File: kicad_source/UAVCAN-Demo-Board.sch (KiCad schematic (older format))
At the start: 35 parts, among them CN1 ARDUINO_NANO_33, CN2 691322310004, CN3 GH_SM04B-GHS-TB, CN4 GH_SM04B-GHS-TB, CN5 691322310004, CN6 691322310004, SW1 TAST_VER, U1 MCP2515, U2 SN65VHD232, U3 DS18B20, Y1 16 MHz

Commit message: started layout, added THT parts
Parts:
- CN5, CN6: footprint CON_wuerth:WR-TBL_691322310004 -> pin_headers:Pin_Header_Straight_1x04
- D1, D2, D3, D5, D6, D7: footprint LEDs:LED_0603 -> LEDs:LED-5MM
- RV1: footprint (none) -> potentiometers:Potentiometer_Trimmer-Piher_PT15-V12-5_horizontal
- U1: footprint SOIC:SOIC-18_7.5x11.6mm_Pitch1.27mm -> DIP:DIP-18_W7.62mm
- U2: footprint SOIC:SOIC-8_3.9x4.9mm_Pitch1.27mm -> DIP:DIP-8_W7.62mm
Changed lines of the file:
@@
 F 0 "U2" H 4775 2887 60  0000 C CNN
 F 1 "SN65VHD232" H 4775 2781 60  0000 C CNN
-F 2 "SOIC:SOIC-8_3.9x4.9mm_Pitch1.27mm" H 5100 1950 60  0001 C CNN
+F 2 "DIP:DIP-8_W7.62mm" H 5100 1950 60  0001 C CNN
 F 3 "" H 4250 2150 60  0000 C CNN
 	1    4250 2000
@@
 F 0 "D1" H 6200 3095 50  0000 C CNN
 F 1 "150060GS75000" H 6200 3186 50  0000 C CNN
-F 2 "LEDs:LED_0603" V 6200 3300 50  0001 C CNN
+F 2 "LEDs:LED-5MM" V 6200 3300 50  0001 C CNN
 F 3 "" V 6200 3300 50  0000 C CNN
 	1    6200 3300
@@
 F 0 "D2" H 6200 3445 50  0000 C CNN
 F 1 "150060RS75000" H 6200 3536 50  0000 C CNN
-F 2 "LEDs:LED_0603" V 6200 3650 50  0001 C CNN
+F 2 "LEDs:LED-5MM" V 6200 3650 50  0001 C CNN
 F 3 "" V 6200 3650 50  0000 C CNN
 	1    6200 3650
@@
 F 0 "D3" H 6200 3795 50  0000 C CNN
 F 1 "150060YS75000" H 6200 3886 50  0000 C CNN
-F 2 "LEDs:LED_0603" V 6200 4000 50  0001 C CNN
+F 2 "LEDs:LED-5MM" V 6200 4000 50  0001 C CNN
 F 3 "" V 6200 4000 50  0000 C CNN
 	1    6200 4000
@@
 F 0 "U1" H 2900 4825 50  0000 C CNN
 F 1 "MCP2515" H 2900 4734 50  0000 C CNN
-F 2 "SOIC:SOIC-18_7.5x11.6mm_Pitch1.27mm" H 2900 4100 50  0001 C CNN
+F 2 "DIP:DIP-18_W7.62mm" H 2900 4100 50  0001 C CNN
 F 3 "" H 2900 4100 50  0001 C CNN
 	1    2900 4100
@@
 F 0 "D5" H 6200 4195 50  0000 C CNN
 F 1 "150060YS75000" H 6200 4286 50  0000 C CNN
-F 2 "LEDs:LED_0603" V 6200 4400 50  0001 C CNN
+F 2 "LEDs:LED-5MM" V 6200 4400 50  0001 C CNN
 F 3 "" V 6200 4400 50  0000 C CNN
 	1    6200 4400
@@
 F 0 "D6" H 6200 4595 50  0000 C CNN
 F 1 "150060YS75000" H 6200 4686 50  0000 C CNN
-F 2 "LEDs:LED_0603" V 6200 4800 50  0001 C CNN
+F 2 "LEDs:LED-5MM" V 6200 4800 50  0001 C CNN
 F 3 "" V 6200 4800 50  0000 C CNN
 	1    6200 4800
@@
 F 0 "D7" H 6200 4995 50  0000 C CNN
 F 1 "150060YS75000" H 6200 5086 50  0000 C CNN
-F 2 "LEDs:LED_0603" V 6200 5200 50  0001 C CNN
+F 2 "LEDs:LED-5MM" V 6200 5200 50  0001 C CNN
 F 3 "" V 6200 5200 50  0000 C CNN
 	1    6200 5200
@@
 F 0 "RV1" V 6104 6372 50  0000 R CNN
 F 1 "POT" V 6195 6372 50  0000 R CNN
-F 2 "" H 6150 6450 50  0000 C CNN
+F 2 "potentiometers:Potentiometer_Trimmer-Piher_PT15-V12-5_horizontal" H 6150 6450 50  0001 C CNN
 F 3 "" H 6150 6450 50  0000 C CNN
 	1    6150 6450
@@
 F 0 "CN5" H 2328 1541 50  0000 L CNN
 F 1 "691322310004" H 2328 1450 50  0000 L CNN
-F 2 "CON_wuerth:WR-TBL_691322310004" H 2250 1500 50  0001 C CNN
+F 2 "pin_headers:Pin_Header_Straight_1x04" H 2250 1500 50  0001 C CNN
 F 3 "" H 2250 1500 50  0000 C CNN
 	1    2250 1500
@@
 F 0 "CN6" H 2328 2491 50  0000 L CNN
 F 1 "691322310004" H 2328 2400 50  0000 L CNN
-F 2 "CON_wuerth:WR-TBL_691322310004" H 2250 2450 50  0001 C CNN
+F 2 "pin_headers:Pin_Header_Straight_1x04" H 2250 2450 50  0001 C CNN
 F 3 "" H 2250 2450 50  0000 C CNN
 	1    2250 2450

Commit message: switched to THT parts
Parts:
- C1: footprint capacitors:C_0603 -> Capacitor_THT:C_Disc_D3.8mm_W2.6mm_P2.50mm
- C2, C3, C4: footprint (none) -> Capacitor_THT:C_Disc_D3.8mm_W2.6mm_P2.50mm
- D4: footprint diodes:SOD-123 -> Diode_THT:D_DO-41_SOD81_P7.62mm_Horizontal
- R1, R2, R3, R4, R5, R6, R7, R8: footprint resistors:R_0603 -> Resistor_THT:R_Axial_DIN0207_L6.3mm_D2.5mm_P7.62mm_Horizontal
- RV1: footprint potentiometers:Potentiometer_Trimmer-Piher_PT15-V12-5_horizontal -> Potentiometer_THT:Potentiometer_Piher_PT-10-V10_Vertical
- Y1: footprint (none) -> crystals:Crystal_HC49-U_Vertical
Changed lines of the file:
@@
 F 0 "R4" H 6659 1996 50  0000 L CNN
 F 1 "DNI" H 6659 1905 50  0000 L CNN
-F 2 "resistors:R_0603" H 6600 1800 50  0001 C CNN
+F 2 "Resistor_THT:R_Axial_DIN0207_L6.3mm_D2.5mm_P7.62mm_Horizontal" H 6600 1800 50  0001 C CNN
 F 3 "" H 6600 1950 50  0000 C CNN
 	1    6600 1950
@@
 F 0 "C1" H 3892 1246 50  0000 L CNN
 F 1 "100nF" H 3892 1155 50  0000 L CNN
-F 2 "capacitors:C_0603" H 3800 1050 50  0001 C CNN
+F 2 "Capacitor_THT:C_Disc_D3.8mm_W2.6mm_P2.50mm" H 3800 1050 50  0001 C CNN
 F 3 "" H 3800 1200 50  0000 C CNN
 	1    3800 1200
@@
 F 0 "D4" H 10200 3605 50  0000 C CNN
 F 1 "DNI" H 10200 3514 50  0000 C CNN
-F 2 "diodes:SOD-123" V 10200 3400 50  0001 C CNN
+F 2 "Diode_THT:D_DO-41_SOD81_P7.62mm_Horizontal" V 10200 3400 50  0001 C CNN
 F 3 "" V 10200 3400 50  0000 C CNN
 	1    10200 3400
@@
 F 0 "R1" H 5709 3346 50  0000 L CNN
 F 1 "1k" H 5709 3255 50  0000 L CNN
-F 2 "resistors:R_0603" H 5650 3150 50  0001 C CNN
+F 2 "Resistor_THT:R_Axial_DIN0207_L6.3mm_D2.5mm_P7.62mm_Horizontal" H 5650 3150 50  0001 C CNN
 F 3 "" H 5650 3300 50  0000 C CNN
 	1    5650 3300
@@
 F 0 "R2" H 5709 3696 50  0000 L CNN
 F 1 "1k" H 5709 3605 50  0000 L CNN
-F 2 "resistors:R_0603" H 5650 3500 50  0001 C CNN
+F 2 "Resistor_THT:R_Axial_DIN0207_L6.3mm_D2.5mm_P7.62mm_Horizontal" H 5650 3500 50  0001 C CNN
 F 3 "" H 5650 3650 50  0000 C CNN
 	1    5650 3650
@@
 F 0 "R3" H 5709 4046 50  0000 L CNN
 F 1 "2k" H 5709 3955 50  0000 L CNN
-F 2 "resistors:R_0603" H 5650 3850 50  0001 C CNN
+F 2 "Resistor_THT:R_Axial_DIN0207_L6.3mm_D2.5mm_P7.62mm_Horizontal" H 5650 3850 50  0001 C CNN
 F 3 "" H 5650 4000 50  0000 C CNN
 	1    5650 4000
@@
 F 0 "Y1" H 3950 4925 50  0000 C CNN
 F 1 "16 MHz" H 3950 4834 50  0000 C CNN
-F 2 "" H 3950 4700 50  0000 C CNN
+F 2 "crystals:Crystal_HC49-U_Vertical" H 3950 4700 50  0001 C CNN
 F 3 "" H 3950 4700 50  0000 C CNN
 	1    3950 4700
@@
 F 0 "C2" H 3692 4896 50  0000 L CNN
 F 1 "18pF" H 3692 4805 50  0000 L CNN
-F 2 "" H 3550 4700 50  0001 C CNN
+F 2 "Capacitor_THT:C_Disc_D3.8mm_W2.6mm_P2.50mm" H 3550 4700 50  0001 C CNN
 F 3 "" H 3600 4850 50  0000 C CNN
 	1    3600 4850
@@
 F 0 "C4" H 4342 4896 50  0000 L CNN
 F 1 "18pF" H 4342 4805 50  0000 L CNN
-F 2 "" H 4200 4700 50  0001 C CNN
+F 2 "Capacitor_THT:C_Disc_D3.8mm_W2.6mm_P2.50mm" H 4200 4700 50  0001 C CNN
 F 3 "" H 4250 4850 50  0000 C CNN
 	1    4250 4850
@@
 F 0 "C3" H 4142 3796 50  0000 L CNN
 F 1 "100nF" H 4142 3705 50  0000 L CNN
-F 2 "" H 4000 3600 50  0001 C CNN
+F 2 "Capacitor_THT:C_Disc_D3.8mm_W2.6mm_P2.50mm" H 4000 3600 50  0001 C CNN
 F 3 "" H 4050 3750 50  0000 C CNN
 	1    4050 3750
@@
 F 0 "R5" H 5709 4446 50  0000 L CNN
 F 1 "1k" H 5709 4355 50  0000 L CNN
-F 2 "resistors:R_0603" H 5650 4250 50  0001 C CNN
+F 2 "Resistor_THT:R_Axial_DIN0207_L6.3mm_D2.5mm_P7.62mm_Horizontal" H 5650 4250 50  0001 C CNN
 F 3 "" H 5650 4400 50  0000 C CNN
 	1    5650 4400
@@
 F 0 "R6" H 5709 4846 50  0000 L CNN
 F 1 "1k" H 5709 4755 50  0000 L CNN
-F 2 "resistors:R_0603" H 5650 4650 50  0001 C CNN
+F 2 "Resistor_THT:R_Axial_DIN0207_L6.3mm_D2.5mm_P7.62mm_Horizontal" H 5650 4650 50  0001 C CNN
 F 3 "" H 5650 4800 50  0000 C CNN
 	1    5650 4800
@@
 F 0 "R7" H 5709 5246 50  0000 L CNN
 F 1 "1k" H 5709 5155 50  0000 L CNN
-F 2 "resistors:R_0603" H 5650 5050 50  0001 C CNN
+F 2 "Resistor_THT:R_Axial_DIN0207_L6.3mm_D2.5mm_P7.62mm_Horizontal" H 5650 5050 50  0001 C CNN
 F 3 "" H 5650 5200 50  0000 C CNN
 	1    5650 5200
@@
 F 0 "RV1" V 6104 6372 50  0000 R CNN
 F 1 "POT" V 6195 6372 50  0000 R CNN
-F 2 "potentiometers:Potentiometer_Trimmer-Piher_PT15-V12-5_horizontal" H 6150 6450 50  0001 C CNN
+F 2 "Potentiometer_THT:Potentiometer_Piher_PT-10-V10_Vertical" H 6150 6450 50  0001 C CNN
 F 3 "" H 6150 6450 50  0000 C CNN
 	1    6150 6450
@@
 F 0 "R8" H 8009 4246 50  0000 L CNN
 F 1 "10k" H 8009 4155 50  0000 L CNN
-F 2 "resistors:R_0603" H 7950 4050 50  0001 C CNN
+F 2 "Resistor_THT:R_Axial_DIN0207_L6.3mm_D2.5mm_P7.62mm_Horizontal" H 7950 4050 50  0001 C CNN
 F 3 "" H 7950 4200 50  0000 C CNN
 	1    7950 4200

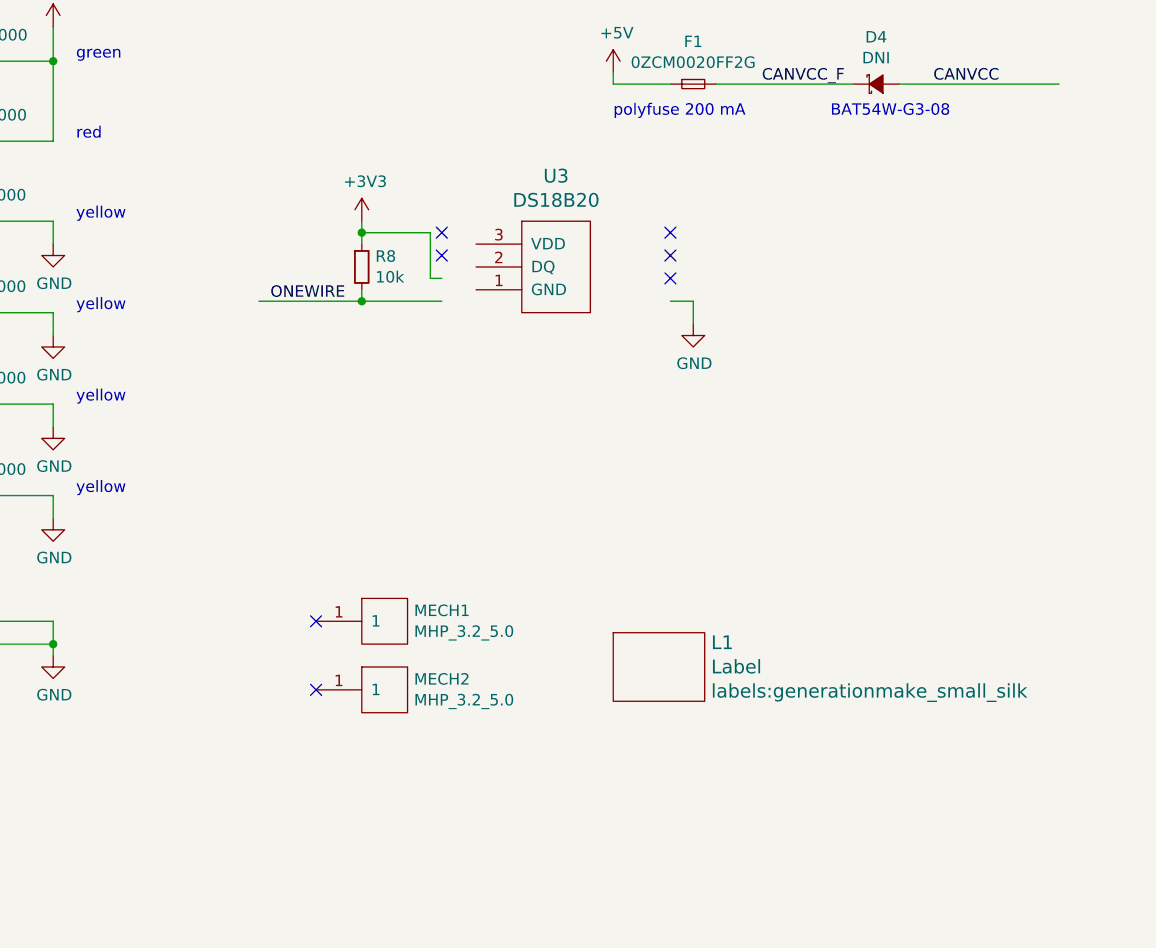
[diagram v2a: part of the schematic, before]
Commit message: changed DS18B20 to TO-92, cleaned up layout, added labels
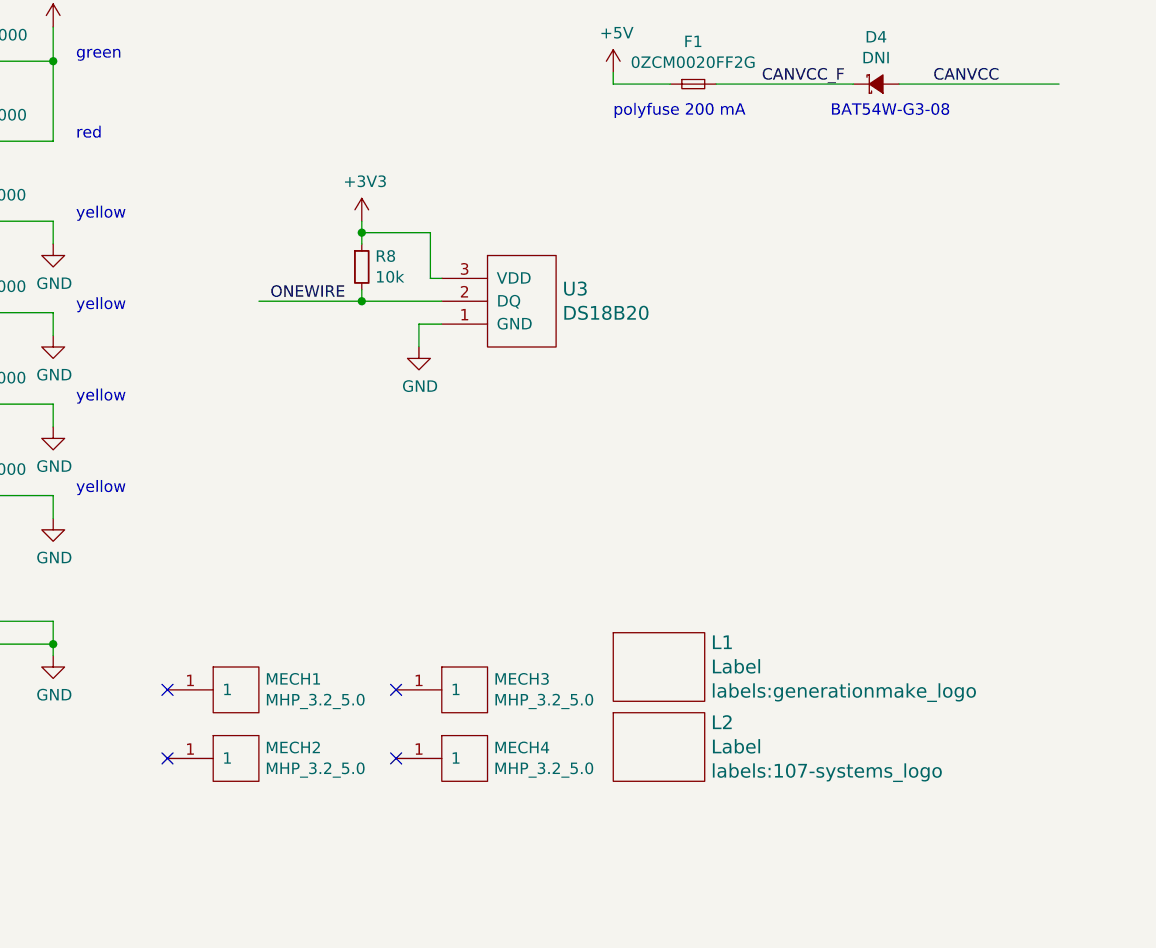
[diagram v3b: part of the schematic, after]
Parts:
- added L2: Label, labels:107-systems_logo, symbol devices:Label
- added MECH3, MECH4: MHP_3.2_5.0, MECH_mounting_holes:MHP_3.2_5.0, symbol MECH_mounting-holes:MHP_3.2_5.0
- F1: footprint resistors:R_0603 -> Resistor_THT:R_Axial_DIN0207_L6.3mm_D2.5mm_P5.08mm_Vertical
- L1: footprint labels:generationmake_small_silk -> labels:generationmake_logo
- U3: footprint SOIC:SOIC-8_3.9x4.9mm_Pitch1.27mm -> Package_TO_SOT_THT:TO-92
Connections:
- no-connect marks 16 -> 13
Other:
- moved on the sheet: MECH1, MECH2
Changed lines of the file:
@@
 F 0 "L1" H 9478 6056 60  0000 L CNN
 F 1 "Label" H 9478 5950 60  0000 L CNN
-F 2 "labels:generationmake_small_silk" H 9478 5844 60  0000 L CNN
+F 2 "labels:generationmake_logo" H 9478 5844 60  0000 L CNN
 F 3 "" H 9250 5950 60  0000 C CNN
 	1    9250 5950
@@
 F 0 "F1" H 9400 3585 50  0000 C CNN
 F 1 "0ZCM0020FF2G" H 9400 3494 50  0000 C CNN
-F 2 "resistors:R_0603" H 9400 3400 50  0001 C CNN
+F 2 "Resistor_THT:R_Axial_DIN0207_L6.3mm_D2.5mm_P5.08mm_Vertical" H 9400 3400 50  0001 C CNN
 F 3 "" H 9400 3400 50  0000 C CNN
 	1    9400 3400
@@
 L MECH_mounting-holes:MHP_3.2_5.0 MECH1
 U 1 1 5FF35FFC
-P 8050 5750
-F 0 "MECH1" H 8178 5796 50  0000 L CNN
-F 1 "MHP_3.2_5.0" H 8178 5705 50  0000 L CNN
-F 2 "MECH_mounting_holes:MHP_3.2_5.0" H 7950 5800 50  0001 C CNN
-F 3 "" H 8050 5750 50  0001 C CNN
-	1    8050 5750
-	1    0    0    -1
-$EndComp
-NoConn ~ 7750 5750
+P 7400 6050
+F 0 "MECH1" H 7528 6096 50  0000 L CNN
+F 1 "MHP_3.2_5.0" H 7528 6005 50  0000 L CNN
+F 2 "MECH_mounting_holes:MHP_3.2_5.0" H 7300 6100 50  0001 C CNN
+F 3 "" H 7400 6050 50  0001 C CNN
+	1    7400 6050
+	1    0    0    -1
+$EndComp
+NoConn ~ 7100 6050
 $Comp
 L MECH_mounting-holes:MHP_3.2_5.0 MECH2
 U 1 1 5FF376EB
-P 8050 6050
-F 0 "MECH2" H 8178 6096 50  0000 L CNN
-F 1 "MHP_3.2_5.0" H 8178 6005 50  0000 L CNN
-F 2 "MECH_mounting_holes:MHP_3.2_5.0" H 7950 6100 50  0001 C CNN
-F 3 "" H 8050 6050 50  0001 C CNN
-	1    8050 6050
-	1    0    0    -1
-$EndComp
-NoConn ~ 7750 6050
+P 7400 6350
+F 0 "MECH2" H 7528 6396 50  0000 L CNN
+F 1 "MHP_3.2_5.0" H 7528 6305 50  0000 L CNN
+F 2 "MECH_mounting_holes:MHP_3.2_5.0" H 7300 6400 50  0001 C CNN
+F 3 "" H 7400 6350 50  0001 C CNN
+	1    7400 6350
+	1    0    0    -1
+$EndComp
+NoConn ~ 7100 6350
 Text Notes 10000 3550 0    50   ~ 0
  BAT54W-G3-08
@@
 I2C_SCL
 $Comp
-L IC_sensor:DS18B20 U3
-U 1 1 60516299
-P 8800 4200
-F 0 "U3" H 8800 4597 60  0000 C CNN
-F 1 "DS18B20" H 8800 4491 60  0000 C CNN
-F 2 "SOIC:SOIC-8_3.9x4.9mm_Pitch1.27mm" H 8700 4350 60  0001 C CNN
-F 3 "" H 8800 4200 60  0000 C CNN
-	1    8800 4200
-	1    0    0    -1
-$EndComp
-$Comp
 L devices:R_0603 R?
 U 1 1 60516B88
@@
 L power-supply:GND #PWR?
 U 1 1 6053070B
-P 9400 4450
+P 8200 4550
 AR Path="/5FD58A5B/6053070B" Ref="#PWR?"  Part="1"
 AR Path="/6053070B" Ref="#PWR029"  Part="1"
-F 0 "#PWR029" H 9400 4200 50  0001 C CNN
-F 1 "GND" H 9405 4277 50  0000 C CNN
-F 2 "" H 9400 4450 50  0000 C CNN
-F 3 "" H 9400 4450 50  0000 C CNN
-	1    9400 4450
-	1    0    0    -1
-$EndComp
-Wire Wire Line
-	9300 4350 9400 4350
-Wire Wire Line
-	9400 4350 9400 4450
-NoConn ~ 9300 4050
-NoConn ~ 9300 4150
-NoConn ~ 9300 4250
-NoConn ~ 8300 4050
-NoConn ~ 8300 4150
+F 0 "#PWR029" H 8200 4300 50  0001 C CNN
+F 1 "GND" H 8205 4377 50  0000 C CNN
+F 2 "" H 8200 4550 50  0000 C CNN
+F 3 "" H 8200 4550 50  0000 C CNN
+	1    8200 4550
+	1    0    0    -1
+$EndComp
 Text Label 7550 4350 0    50   ~ 0
 ONEWIRE
@@
 SERIAL_RX
 NoConn ~ 1350 5850
+$Comp
+L IC_sensor:DS18B20 U3
+U 1 1 6043C9C6
+P 8650 4350
+F 0 "U3" H 8828 4403 60  0000 L CNN
+F 1 "DS18B20" H 8828 4297 60  0000 L CNN
+F 2 "Package_TO_SOT_THT:TO-92" H 8700 4550 60  0001 C CNN
+F 3 "" H 8650 4350 60  0000 C CNN
+	1    8650 4350
+	1    0    0    -1
+$EndComp
+Wire Wire Line
+	8300 4450 8200 4450
+Wire Wire Line
+	8200 4450 8200 4550
+$Comp
+L MECH_mounting-holes:MHP_3.2_5.0 MECH3
+U 1 1 60474D54
+P 8400 6050
+F 0 "MECH3" H 8528 6096 50  0000 L CNN
+F 1 "MHP_3.2_5.0" H 8528 6005 50  0000 L CNN
+F 2 "MECH_mounting_holes:MHP_3.2_5.0" H 8300 6100 50  0001 C CNN
+F 3 "" H 8400 6050 50  0001 C CNN
+	1    8400 6050
+	1    0    0    -1
+$EndComp
+NoConn ~ 8100 6050
+$Comp
+L MECH_mounting-holes:MHP_3.2_5.0 MECH4
+U 1 1 60474F85
+P 8400 6350
+F 0 "MECH4" H 8528 6396 50  0000 L CNN
+F 1 "MHP_3.2_5.0" H 8528 6305 50  0000 L CNN
+F 2 "MECH_mounting_holes:MHP_3.2_5.0" H 8300 6400 50  0001 C CNN
+F 3 "" H 8400 6350 50  0001 C CNN
+	1    8400 6350
+	1    0    0    -1
+$EndComp
+NoConn ~ 8100 6350
+$Comp
+L devices:Label L?
+U 1 1 6048009E
+P 9250 6300
+AR Path="/5FD58A5B/6048009E" Ref="L?"  Part="1"
+AR Path="/6048009E" Ref="L2"  Part="1"
+F 0 "L2" H 9478 6406 60  0000 L CNN
+F 1 "Label" H 9478 6300 60  0000 L CNN
+F 2 "labels:107-systems_logo" H 9478 6194 60  0000 L CNN
+F 3 "" H 9250 6300 60  0000 C CNN
+	1    9250 6300
+	1    0    0    -1
+$EndComp
 $EndSCHEMATC
